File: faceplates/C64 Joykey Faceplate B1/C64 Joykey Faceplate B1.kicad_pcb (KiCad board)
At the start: 2 copper layers, 99.7 x 74.9 mm, 5 parts, among them M1 Mounting, M2 Mounting, M3 Mounting, M4 Mounting

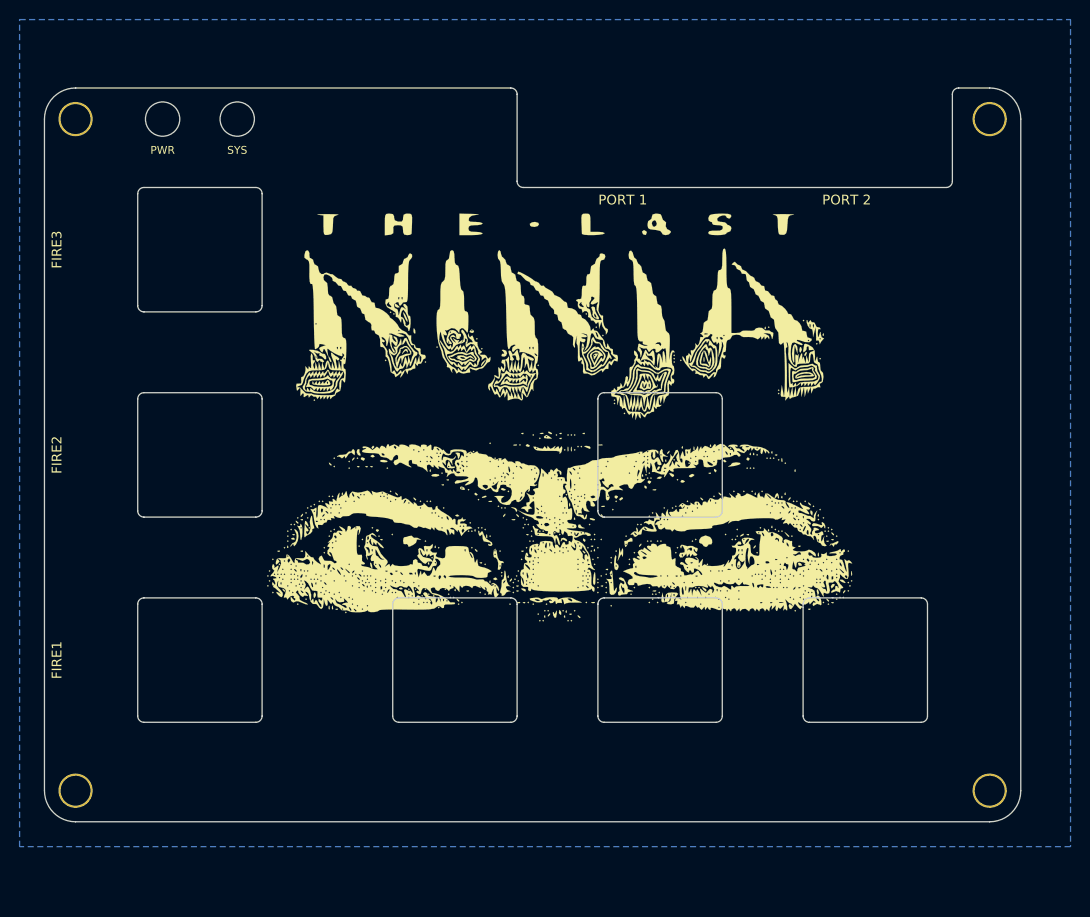
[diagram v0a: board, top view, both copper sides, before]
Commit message: Faceplate B1 update
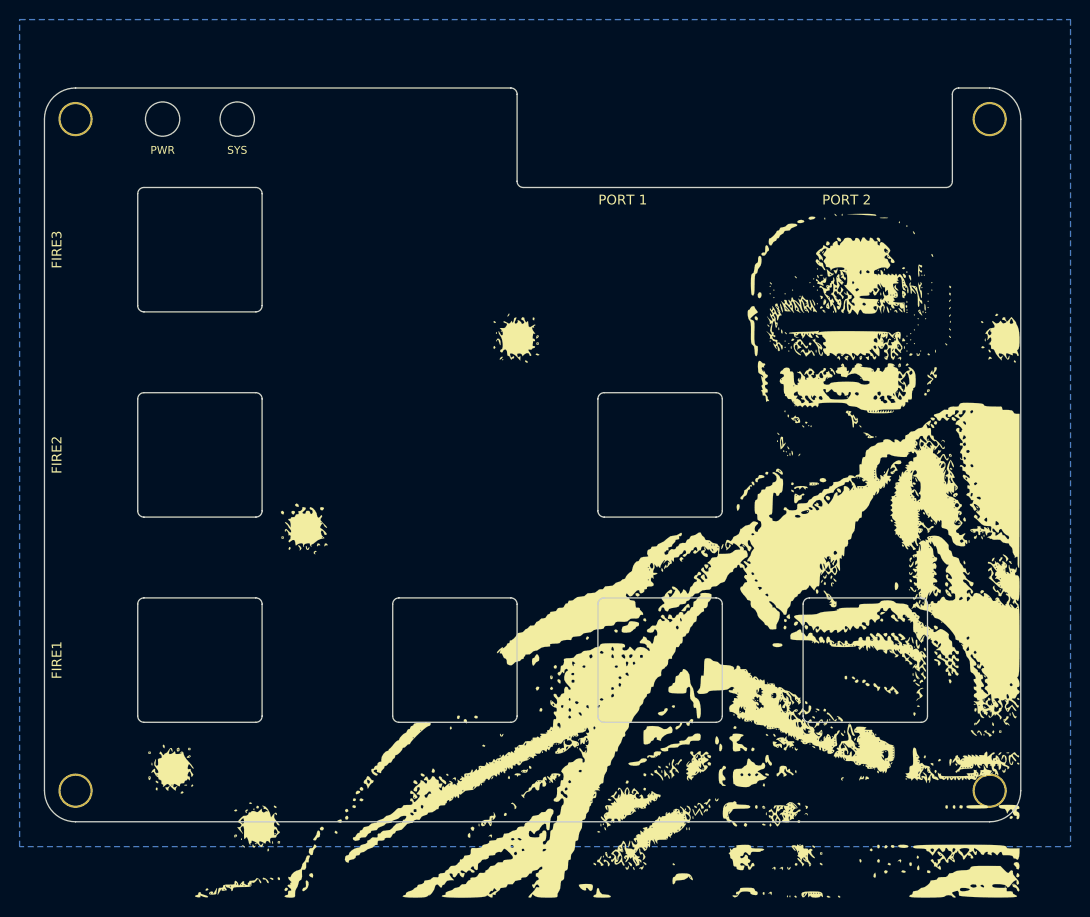
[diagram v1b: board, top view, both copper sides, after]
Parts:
- removed the G*** at (193.7, 116.2)
- added G***: LOGO, artwork:robocop, F.Cu at (193.5, 130.0)
